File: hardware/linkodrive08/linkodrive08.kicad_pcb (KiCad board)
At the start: 4 copper layers, 143 parts, among them J1 USB_C_Receptacle_USB2.0_16P, J10 WCH_GPIO, J11 ENC, J12 LKS_SPI, J13 LKS_I2C, J14 WCH_UART_ALT, J15 LKS_SIF, J16 LKS_IO, J2 HALL, J3 WCH_SWD, J4 LKS_SWD, J5 MOT_POWER, J6 GATE_DRIVE, J7 LOGIC_POWER, J8 MOT, J9 CAN, Q1 HSU6066, Q2 HSU6066, Q3 HSU6066, Q4 HSU6066, Q5 HSU6066, Q6 HSU6066, U1 LKS32MC086NxQx, U2 CH32V203G6U6, U3 XL1509-ADJ, U4 SN65HVD230, U5 LGS5145, Y1 OSC

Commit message: Work on pcb and some parts changes
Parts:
- added C33: 100u, Capacitor_SMD:C_Elec_10x10.2, F.Cu at (249.4, 76.2)
- added C34: 100u, Capacitor_SMD:C_Elec_10x10.2, F.Cu at (249.4, 88.0)
- added C35: 100u, Capacitor_SMD:C_Elec_10x10.2, F.Cu at (249.4, 99.9)
- D1, D10, D4, D7: value SS34 -> C28646289; footprint Diode_SMD:D_SMA -> Diode_SMD:D_SOD-123F
- D2, D3, D5, D6, D8, D9: value ES2DB -> ES2JW; footprint Diode_SMD:D_SMB -> Diode_SMD:D_SOD-123F
- J3: moved to B.Cu
- Q1, Q2, Q3, Q4, Q5, Q6: footprint Package_TO_SOT_SMD:TO-252-2 -> Package_SO:ONSemi_SO-8FL_488AA
- Y1: value OSC -> Crystal_GND24_Small
- moved Q5 103.9 mm to (167.3, 102.3), turned to 90 degrees
- moved C28 103.7 mm to (116.0, 100.8)
- moved J5 103.0 mm to (133.5, 72.6), turned to -90 degrees
- moved R15 99.3 mm to (151.2, 92.8)
- moved Q6 98.3 mm to (177.7, 102.4), turned to 90 degrees
- moved R16 97.5 mm to (148.0, 92.8)
- moved J13 95.5 mm to (112.0, 72.9)
- moved Q1 94.0 mm to (167.5, 72.6), turned to 90 degrees
- moved Q3 93.0 mm to (167.3, 86.6), turned to 90 degrees
- moved D5 91.7 mm to (150.4, 90.8)
- moved R17 90.3 mm to (151.2, 97.4)
- moved Q4 85.1 mm to (177.7, 86.6), turned to 90 degrees
- moved D6 81.7 mm to (150.4, 95.2)
- moved R19 81.4 mm to (148.0, 97.4)
- moved Q2 78.7 mm to (177.7, 72.6), turned to 90 degrees
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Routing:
- net /UART_ALT_TX: track 0.00 -> 34.7 mm, vias 0 -> 4
- net Net-(Q4-G): track 0.00 -> 31.9 mm
- net /UART_ALT_RX: track 0.00 -> 31.2 mm, vias 0 -> 3
- net /ISENSE_TOT+: track 0.00 -> 27.8 mm
- net /ISENSE_TOT-: track 0.00 -> 26.9 mm
- net /PB1: track 0.00 -> 22.5 mm, vias 0 -> 3
- net /LKS_SWCLK: track 5.28 -> 26.6 mm
- net Net-(Q3-G): track 0.00 -> 20.3 mm
- net /PA4: track 0.00 -> 20.2 mm, vias 0 -> 3
- net Net-(JP4-A): track 0.00 -> 19.9 mm
- net /PB3: track 0.00 -> 19.2 mm
- net /WCH_SWDIO: track 0.00 -> 18.6 mm, vias 0 -> 5
- net /WCH_SWCLK: track 0.00 -> 17.8 mm, vias 0 -> 5
- net /WCH_BOOT0: track 0.00 -> 17.8 mm, vias 0 -> 2
- net /PA0: track 2.91 -> 18.1 mm, vias 1 -> 2
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
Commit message: more work on PCB
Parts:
- U2: footprint Package_DFN_QFN:QFN-28-1EP_4x4mm_P0.4mm_EP2.6x2.6mm -> Package_DFN_QFN:QFN-28-1EP_4x4mm_P0.4mm_EP2.6x2.6mm_ThermalVias
- moved R41 115.2 mm to (97.5, 83.0), turned to -90 degrees
- moved R42 115.1 mm to (98.0, 86.3), turned to -90 degrees
- moved C37 111.5 mm to (99.1, 83.1), turned to 90 degrees
- moved TP3 11.4 mm to (101.1, 86.0)
- moved TP6 2.93 mm to (118.4, 100.3)
- moved TP4 0.76 mm to (91.3, 94.5)
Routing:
- net GND: track 54.5 -> 265.1 mm, vias 3 -> 21
- net +3V3: track 42.8 -> 164.4 mm, vias 1 -> 9
- net VBUS: track 0.00 -> 49.1 mm, vias 0 -> 3
- net /SPI_DI: track 0.00 -> 45.6 mm, vias 0 -> 4
- net Vdrive: track 8.61 -> 53.4 mm, vias 1 -> 4
- net /LED1: track 0.00 -> 37.3 mm, vias 0 -> 8
- net /HALL_V: track 0.00 -> 35.5 mm, vias 0 -> 4
- net /P2.2: track 0.00 -> 31.6 mm, vias 0 -> 2
- net /HALL_U: track 0.00 -> 30.1 mm, vias 0 -> 5
- net /CAN_TX: track 0.00 -> 30.1 mm, vias 0 -> 4
- net /LKS_~{RST}: track 0.40 -> 29.6 mm, vias 1 -> 8
- net /HALL_W: track 0.00 -> 29.0 mm, vias 0 -> 3
- net /I2C_SCL: track 0.00 -> 28.4 mm, vias 0 -> 4
- net /UART_RX: track 0.00 -> 27.8 mm, vias 0 -> 4
- net /CAN_RX: track 0.00 -> 25.9 mm, vias 0 -> 2
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
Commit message: Finish layout
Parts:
- removed the J5 at (133.5, 72.6)
- removed the J8 at (279.8, 77.2)
- added C38: Cs, Capacitor_SMD:C_0603_1608Metric, F.Cu at (137.4, 95.0)
- added J1: VBUS, TestPoint:TestPoint_Plated_Hole_D4.0mm, F.Cu at (117.1, 129.5)
- added J14: MOT_U, TestPoint:TestPoint_Plated_Hole_D4.0mm, F.Cu at (129.0, 154.2)
- added J15: MOT_V, TestPoint:TestPoint_Plated_Hole_D4.0mm, F.Cu at (107.4, 154.4)
- added J16: MOT_W, TestPoint:TestPoint_Plated_Hole_D4.0mm, F.Cu at (85.3, 154.4)
- added J19: GND, TestPoint:TestPoint_Plated_Hole_D4.0mm, F.Cu at (132.1, 96.3)
- added R46: Rs, Resistor_SMD:R_0603_1608Metric, F.Cu at (136.6, 97.4)
- added R47: Rs, Resistor_SMD:R_0603_1608Metric, F.Cu at (138.2, 97.4)
- D12: renamed from D10; value C28646289 -> DSK310
- D3: renamed from D4; value C28646289 -> DSK310
- D4: renamed from D1; value C28646289 -> DSK310
- D9: renamed from D7; value C28646289 -> DSK310
- JP1, JP2: moved to B.Cu
- Q1: renamed from Q3; value HSU6066 -> JMTK80N06A; footprint Package_SO:ONSemi_SO-8FL_488AA -> Package_TO_SOT_SMD:TO-252-2
- Q2: renamed from Q4; value HSU6066 -> JMTK80N06A; footprint Package_SO:ONSemi_SO-8FL_488AA -> Package_TO_SOT_SMD:TO-252-2
- Q3: renamed from Q1; value HSU6066 -> JMTK80N06A; footprint Package_SO:ONSemi_SO-8FL_488AA -> Package_TO_SOT_SMD:TO-252-2
- Q4: renamed from Q2; value HSU6066 -> JMTK80N06A; footprint Package_SO:ONSemi_SO-8FL_488AA -> Package_TO_SOT_SMD:TO-252-2
- Q5, Q6: value HSU6066 -> JMTK80N06A; footprint Package_SO:ONSemi_SO-8FL_488AA -> Package_TO_SOT_SMD:TO-252-2
- moved R20 172.0 mm to (81.2, 131.6)
- moved C24 171.9 mm to (78.5, 118.6), turned to 90 degrees
- moved D7 162.7 mm to (88.4, 122.0)
- moved R14 157.3 mm to (86.0, 128.3)
- moved D8 156.1 mm to (88.5, 126.3)
- moved C23 154.9 mm to (97.5, 118.6), turned to 90 degrees
- moved C14 151.7 mm to (87.3, 132.3), turned to 90 degrees
- moved C13 150.8 mm to (91.2, 133.0), turned to 180 degrees
- moved R18 150.8 mm to (89.2, 128.3), turned to 180 degrees
- moved C22 145.3 mm to (89.0, 114.0), turned to 90 degrees
- moved R17 141.8 mm to (89.2, 124.0), turned to 180 degrees
- moved R13 139.5 mm to (86.0, 124.0)
- moved C20 137.2 mm to (119.0, 118.9), turned to 90 degrees
- moved R27 136.6 mm to (89.0, 117.0), turned to 90 degrees
- moved NT5 135.3 mm to (80.4, 128.6), turned to 90 degrees
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- renumbered C29 to C10, C5 to C13, C7 to C14, C28 to C15, C2 to C16, C3 to C17, C25 to C18, C24 to C19, C37 to C2, C33 to C20, C13 to C21, C8 to C22, C34 to C23, C35 to C24, C36 to C25, C14 to C26, C30 to C27, C15 to C28, C19 to C29, C9 to C3, C16 to C30, C17 to C31, C22 to C32, C26 to C33, C21 to C34, C18 to C35, C20 to C36, C23 to C37, C10 to C5, C27 to C7, C31 to C8, C32 to C9, D12 to D1, D8 to D10, D9 to D11, D11 to D13, D13 to D2, D2 to D7, D3 to D8, J11 to J10, J13 to J11, J4 to J12, J2 to J13, J10 to J17, J14 to J18, J1 to J2, J6 to J3, J7 to J4, J15 to J5, J16 to J6, J12 to J7, J9 to J8, J3 to J9, NT9 to NT1, NT7 to NT10, NT8 to NT11, NT10 to NT2, NT1 to NT3, NT2 to NT4, NT3 to NT5, NT4 to NT6, NT5 to NT7, NT6 to NT8, NT11 to NT9, R45 to R1, R5 to R10, R16 to R11, R19 to R12, R7 to R13, R9 to R14, R17 to R16, R6 to R17, R8 to R18, R21 to R19, R1 to R2, R10 to R20, R36 to R21, R37 to R22, R32 to R23, R35 to R24, R18 to R25, R20 to R26, R11 to R27, R12 to R28, R4 to R29, R2 to R3, R43 to R30, R13 to R31, R22 to R32, R24 to R33, R27 to R34, R23 to R35, R25 to R36, R29 to R37, R39 to R38, R40 to R39, R44 to R4, R26 to R40, R28 to R41, R30 to R42, R31 to R43, R33 to R44, R34 to R45, R38 to R5, R41 to R6, R42 to R7, R3 to R8, R14 to R9, TP3 to TP1, TP4 to TP2, TP5 to TP3, TP6 to TP4, TP2 to TP5, TP1 to TP6, U4 to U2, U2 to U3, U3 to U4
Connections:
- C28 pad 2: /VS1 -> /MOT1_MEAS
- C5 pad 2: /VS2 -> /MOT2_MEAS
- C6 pad 2: /VS3 -> /MOT3_MEAS
- NT1 pad 1: /VS2 -> /MOT2_MEAS
- NT2 pad 1: /VS3 -> /MOT3_MEAS
- NT7 pad 1: /ISENSE_TOT- -> /P_IST-
- NT8 pad 2: /ISENSE_TOT+ -> /P_IST+
- NT9 pad 1: /VS1 -> /MOT1_MEAS
- R25 pad 1: /MOT2 -> /MOT2_MEAS
- R27 pad 1: /MOT3 -> /MOT3_MEAS
- R40 pad 1: /MOT1 -> /MOT1_MEAS
- U1 pad 26: /VS1 -> /MOT1_MEAS
- U1 pad 29: /VS2 -> /MOT2_MEAS
- U1 pad 32: /VS3 -> /MOT3_MEAS
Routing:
- net /MOT3_MEAS: track 0.00 -> 77.2 mm, vias 0 -> 4
- net /HO3: track 0.00 -> 58.7 mm, vias 0 -> 9
- net Vdrive: track 53.4 -> 111.3 mm, vias 4 -> 9
- net GND: track 265.1 -> 318.7 mm, vias 21 -> 225
- net /MOT2_MEAS: track 0.00 -> 49.5 mm, vias 0 -> 4
- net /LO3: track 5.76 -> 53.9 mm, vias 0 -> 9
- net /MOT1_MEAS: track 0.00 -> 45.1 mm, vias 0 -> 2
- net /HO1: track 0.00 -> 43.3 mm, vias 0 -> 4
- net /P_ISW-: track 0.00 -> 43.2 mm, vias 0 -> 2
- net /P_ISW+: track 0.00 -> 43.0 mm, vias 0 -> 2
- net /V_U: track 1.36 -> 43.5 mm, vias 1 -> 4
- net /V_W: track 1.33 -> 42.7 mm, vias 1 -> 2
- net /HO2: track 2.77 -> 43.2 mm, vias 0 -> 6
- net /LO1: track 6.51 -> 42.4 mm, vias 0 -> 2
- net /LO2: track 8.98 -> 42.0 mm, vias 0 -> 2
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- added copper zone on B.Cu, net /MOT1
- added copper zone on F.Cu, net /MOT1
- added copper zone on In1.Cu, net /MOT1
- added copper zone on In2.Cu, net /MOT1
- added copper zone on B.Cu, net /MOT2
- added copper zone on F.Cu, net /MOT2
- added copper zone on In1.Cu, net /MOT2
- added copper zone on In2.Cu, net /MOT2
- added copper zone on B.Cu, net /MOT3
- added copper zone on F.Cu, net /MOT3
- added copper zone on In1.Cu, net /MOT3
- added copper zone on In2.Cu, net /MOT3
- added copper zone on B.Cu, net GND
- added copper zone on F.Cu, net GND
- added copper zone on In1.Cu, net GND
- added copper zone on In2.Cu, net GND
- added copper zone on B.Cu, net GNDPWR
- added copper zone on F.Cu, net GNDPWR
- added copper zone on In2.Cu, net GNDPWR
- added copper zone on F.Cu, net VBUS
- added copper zone on In1.Cu, net VBUS
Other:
- board outline added: 67.2 x 90.4 mm

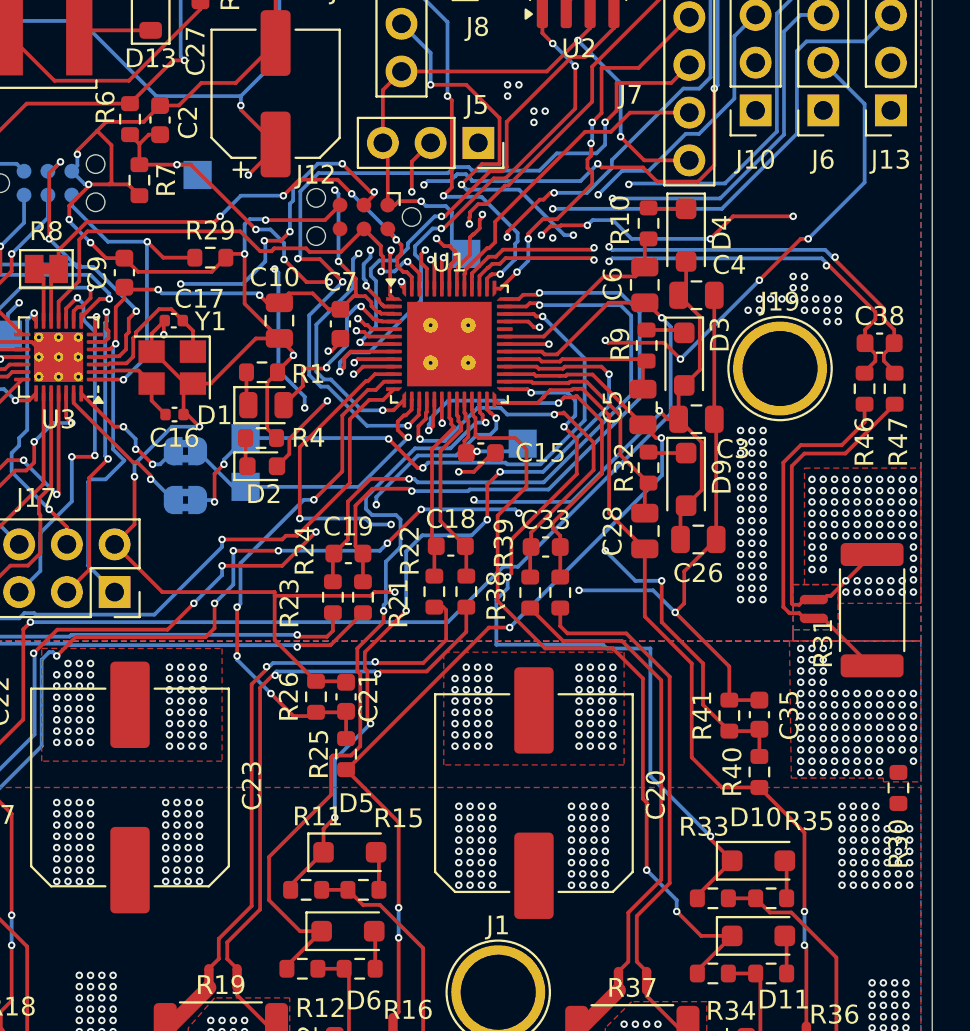
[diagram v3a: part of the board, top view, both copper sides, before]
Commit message: Add power indicator LEDs
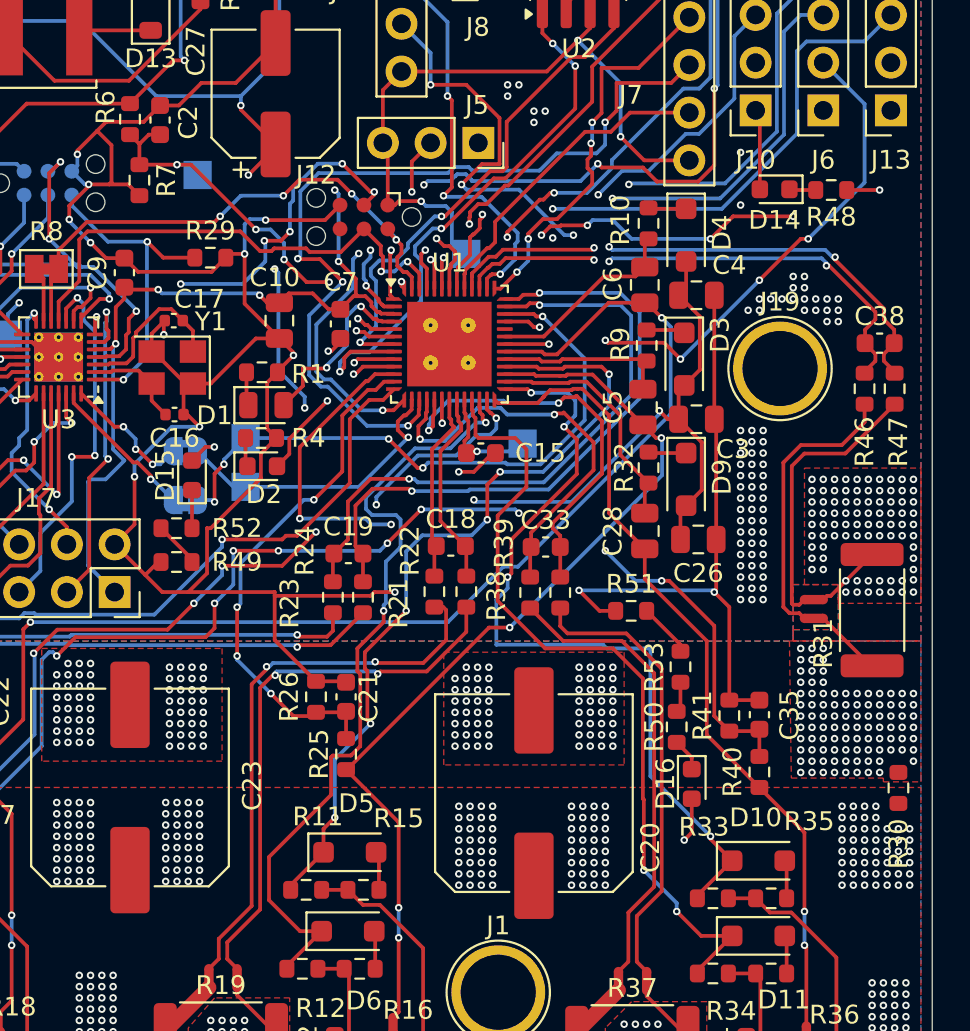
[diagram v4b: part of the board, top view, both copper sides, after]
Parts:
- added D14: LED_Y, LED_SMD:LED_0603_1608Metric, F.Cu at (131.8, 86.8)
- added D15: LED_Y, LED_SMD:LED_0603_1608Metric, F.Cu at (100.8, 102.0)
- added D16: LED_Y, LED_SMD:LED_0603_1608Metric, F.Cu at (127.4, 118.4)
- added R48: 1k, Resistor_SMD:R_0603_1608Metric, F.Cu at (134.8, 86.8)
- added R49: 1k, Resistor_SMD:R_0603_1608Metric, F.Cu at (100.0, 106.6)
- added R50: 1k, Resistor_SMD:R_0603_1608Metric, F.Cu at (126.6, 115.4)
- added R51: 1k, Resistor_SMD:R_0603_1608Metric, F.Cu at (124.2, 109.2)
- added R52: 1k, Resistor_SMD:R_0603_1608Metric, F.Cu at (100.0, 104.8)
- added R53: 1k, Resistor_SMD:R_0603_1608Metric, F.Cu at (126.8, 112.2)
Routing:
- net GND: track 318.7 -> 334.0 mm, vias 225 -> 228
- net Vdrive: track 111.3 -> 118.4 mm, vias 9 -> 10
- net +3V3: track 173.2 -> 177.2 mm
- net Net-(R51-Pad2): track 0.00 -> 2.90 mm
- net VBUS: track 68.8 -> 71.2 mm, vias 469 -> 470
- net Net-(R49-Pad2): track 0.00 -> 2.33 mm
- net Net-(D15-K): track 0.00 -> 2.02 mm
- net Net-(D16-K): track 0.00 -> 1.76 mm
- net Net-(D14-K): track 0.00 -> 1.36 mm
- net Net-(R50-Pad1): track 0.00 -> 1.35 mm
- net /MOT1_MEAS: track 45.1 -> 43.9 mm

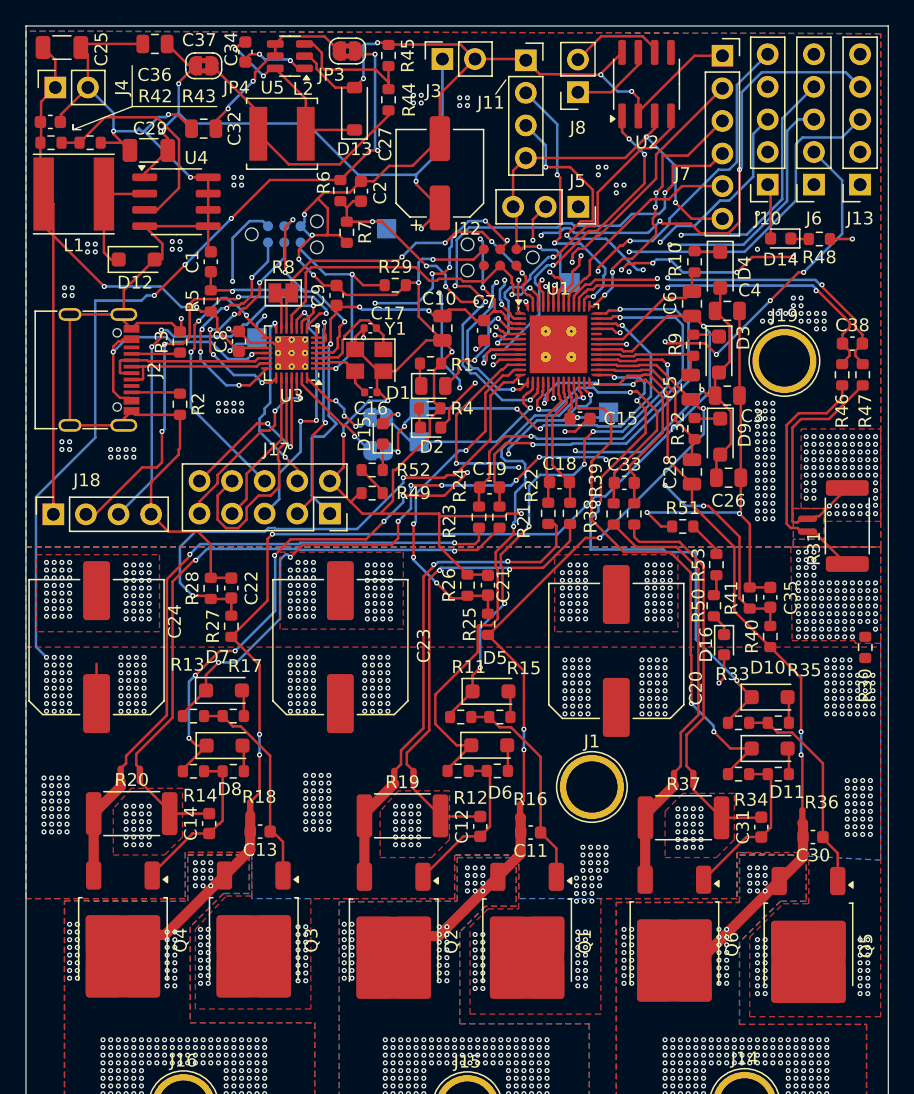
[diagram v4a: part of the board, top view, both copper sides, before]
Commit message: Setup thermal relief on most parts
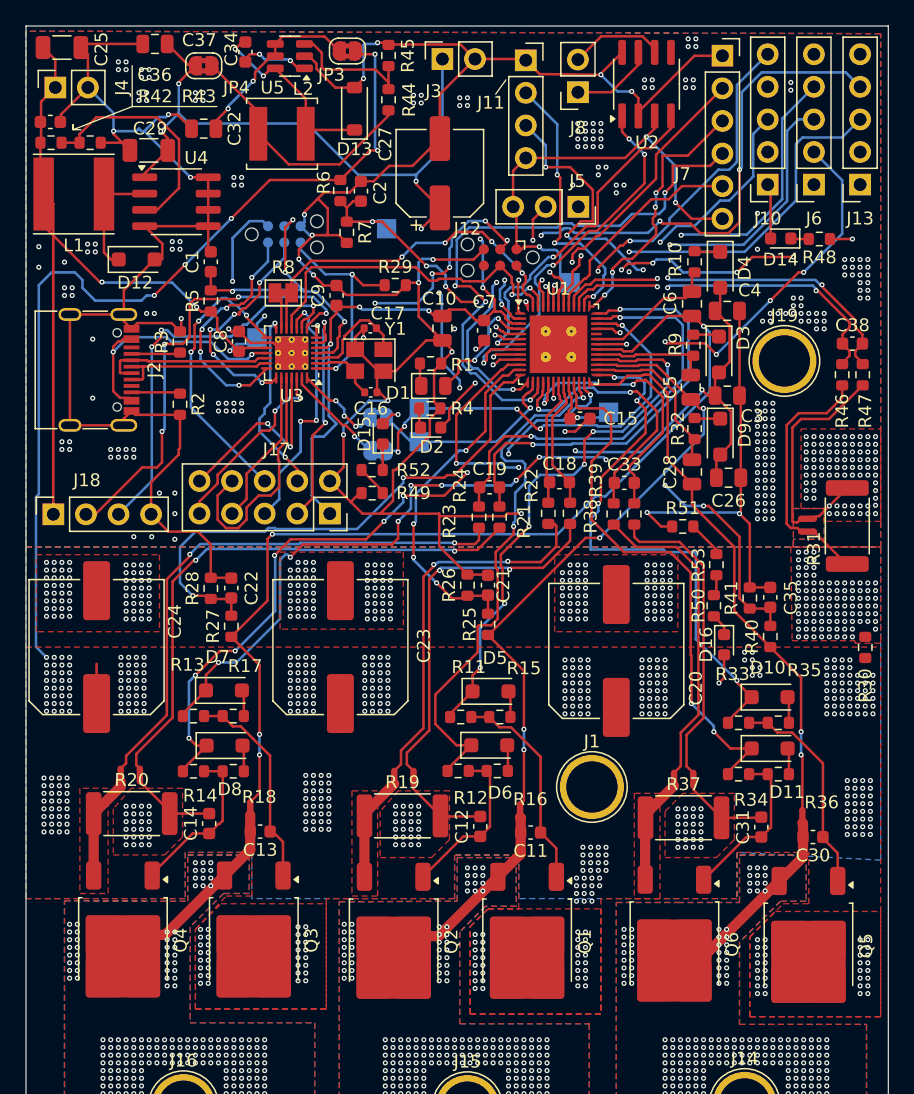
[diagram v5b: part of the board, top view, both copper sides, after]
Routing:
- net VBUS: track 71.2 -> 76.7 mm, vias 470 -> 478
- net GND: vias 228 -> 307
- added copper zone on F.Cu, net Net-(Q2-S)
- added copper zone on F.Cu, net Net-(Q4-S)
- added copper zone on F.Cu, net Net-(Q6-S)
